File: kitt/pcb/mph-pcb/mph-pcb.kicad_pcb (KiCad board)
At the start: 4 copper layers, 280 x 125 mm, 10 parts

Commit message: changed pegboard holes to m5
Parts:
- PEG1, PEG2, PEG3, PEG4: value MountingHole_6.4mm_M6 -> MountingHole_5.3mm_M5; footprint MountingHole:MountingHole_6.4mm_M6 -> MountingHole:MountingHole_5.3mm_M5
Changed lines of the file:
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@@
     (uvia_drill 0.1)
   )
-  (module MountingHole:MountingHole_6.4mm_M6 (layer F.Cu)
+  (module MountingHole:MountingHole_5.3mm_M5 (layer F.Cu)
     (at 286.7 52.05)
-    (descr "Mounting Hole 6.4mm, no annular, M6")
-    (tags "mounting hole 6.4mm no annular m6")
+    (descr "Mounting Hole 5.3mm, no annular, M5")
+    (tags "mounting hole 5.3mm no annular m5")
     (attr virtual)
     (fp_text reference PEG2 (at 0 -7.4) (layer F.SilkS)
       (effects (font (size 1 1) (thickness 0.15)))
     )
-    (fp_text value MountingHole_6.4mm_M6 (at 0 7.4) (layer F.Fab)
+    (fp_text value MountingHole_5.3mm_M5 (at 0 7.4) (layer F.Fab)
       (effects (font (size 1 1) (thickness 0.15)))
     )
-    (fp_circle (center 0 0) (end 6.4 0) (layer Cmts.User) (width 0.15))
-    (fp_circle (center 0 0) (end 6.65 0) (layer F.CrtYd) (width 0.05))
     (fp_text user %R (at 0.3 0) (layer F.Fab)
       (effects (font (size 1 1) (thickness 0.15)))
     )
-    (pad 1 np_thru_hole circle (at 0 0) (size 6.4 6.4) (drill 6.4) (layers *.Cu *.Mask))
+    (fp_circle (center 0 0) (end 5.3 0) (layer Cmts.User) (width 0.15))
+    (fp_circle (center 0 0) (end 5.55 0) (layer F.CrtYd) (width 0.05))
+    (pad 1 np_thru_hole circle (at 0 0) (size 5.3 5.3) (drill 5.3) (layers *.Cu *.Mask))
   )
-  (module MountingHole:MountingHole_6.4mm_M6 (layer F.Cu)
+  (module MountingHole:MountingHole_5.3mm_M5 (layer F.Cu)
     (at 261.3 153.65)
-    (descr "Mounting Hole 6.4mm, no annular, M6")
-    (tags "mounting hole 6.4mm no annular m6")
+    (descr "Mounting Hole 5.3mm, no annular, M5")
+    (tags "mounting hole 5.3mm no annular m5")
     (attr virtual)
     (fp_text reference PEG4 (at 0 -7.4) (layer F.SilkS)
       (effects (font (size 1 1) (thickness 0.15)))
     )
-    (fp_text value MountingHole_6.4mm_M6 (at 0 7.4) (layer F.Fab)
+    (fp_text value MountingHole_5.3mm_M5 (at 0 7.4) (layer F.Fab)
       (effects (font (size 1 1) (thickness 0.15)))
     )
-    (fp_circle (center 0 0) (end 6.4 0) (layer Cmts.User) (width 0.15))
-    (fp_circle (center 0 0) (end 6.65 0) (layer F.CrtYd) (width 0.05))
     (fp_text user %R (at 0.3 0) (layer F.Fab)
       (effects (font (size 1 1) (thickness 0.15)))
     )
-    (pad 1 np_thru_hole circle (at 0 0) (size 6.4 6.4) (drill 6.4) (layers *.Cu *.Mask))
+    (fp_circle (center 0 0) (end 5.3 0) (layer Cmts.User) (width 0.15))
+    (fp_circle (center 0 0) (end 5.55 0) (layer F.CrtYd) (width 0.05))
+    (pad 1 np_thru_hole circle (at 0 0) (size 5.3 5.3) (drill 5.3) (layers *.Cu *.Mask))
   )
-  (module MountingHole:MountingHole_6.4mm_M6 (layer F.Cu)
+  (module MountingHole:MountingHole_5.3mm_M5 (layer F.Cu)
     (at 58.1 77.45)
-    (descr "Mounting Hole 6.4mm, no annular, M6")
-    (tags "mounting hole 6.4mm no annular m6")
+    (descr "Mounting Hole 5.3mm, no annular, M5")
+    (tags "mounting hole 5.3mm no annular m5")
     (attr virtual)
     (fp_text reference PEG1 (at 0 -7.4) (layer F.SilkS)
       (effects (font (size 1 1) (thickness 0.15)))
     )
-    (fp_text value MountingHole_6.4mm_M6 (at 0 7.4) (layer F.Fab)
+    (fp_text value MountingHole_5.3mm_M5 (at 0 7.4) (layer F.Fab)
       (effects (font (size 1 1) (thickness 0.15)))
     )
-    (fp_circle (center 0 0) (end 6.4 0) (layer Cmts.User) (width 0.15))
-    (fp_circle (center 0 0) (end 6.65 0) (layer F.CrtYd) (width 0.05))
     (fp_text user %R (at 0.3 0) (layer F.Fab)
       (effects (font (size 1 1) (thickness 0.15)))
     )
-    (pad 1 np_thru_hole circle (at 0 0) (size 6.4 6.4) (drill 6.4) (layers *.Cu *.Mask))
+    (fp_circle (center 0 0) (end 5.3 0) (layer Cmts.User) (width 0.15))
+    (fp_circle (center 0 0) (end 5.55 0) (layer F.CrtYd) (width 0.05))
+    (pad 1 np_thru_hole circle (at 0 0) (size 5.3 5.3) (drill 5.3) (layers *.Cu *.Mask))
   )
-  (module MountingHole:MountingHole_6.4mm_M6 (layer F.Cu)
+  (module MountingHole:MountingHole_5.3mm_M5 (layer F.Cu)
     (at 58.1 153.65)
-    (descr "Mounting Hole 6.4mm, no annular, M6")
-    (tags "mounting hole 6.4mm no annular m6")
+    (descr "Mounting Hole 5.3mm, no annular, M5")
+    (tags "mounting hole 5.3mm no annular m5")
     (attr virtual)
     (fp_text reference PEG3 (at 0 -7.4) (layer F.SilkS)
       (effects (font (size 1 1) (thickness 0.15)))
     )
-    (fp_text value MountingHole_6.4mm_M6 (at 0 7.4) (layer F.Fab)
+    (fp_text value MountingHole_5.3mm_M5 (at 0 7.4) (layer F.Fab)
       (effects (font (size 1 1) (thickness 0.15)))
     )
-    (fp_circle (center 0 0) (end 6.4 0) (layer Cmts.User) (width 0.15))
-    (fp_circle (center 0 0) (end 6.65 0) (layer F.CrtYd) (width 0.05))
     (fp_text user %R (at 0.3 0) (layer F.Fab)
       (effects (font (size 1 1) (thickness 0.15)))
     )
-    (pad 1 np_thru_hole circle (at 0 0) (size 6.4 6.4) (drill 6.4) (layers *.Cu *.Mask))
+    (fp_circle (center 0 0) (end 5.3 0) (layer Cmts.User) (width 0.15))
+    (fp_circle (center 0 0) (end 5.55 0) (layer F.CrtYd) (width 0.05))
+    (pad 1 np_thru_hole circle (at 0 0) (size 5.3 5.3) (drill 5.3) (layers *.Cu *.Mask))
   )
   (module MountingHole:MountingHole_3.2mm_M3 (layer F.Cu)
@@
       (effects (font (size 1 1) (thickness 0.15)))
     )
+    (fp_circle (center 0 0) (end 3.2 0) (layer Cmts.User) (width 0.15))
     (fp_circle (center 0 0) (end 3.45 0) (layer F.CrtYd) (width 0.05))
-    (fp_circle (center 0 0) (end 3.2 0) (layer Cmts.User) (width 0.15))
     (fp_text user %R (at 0.3 0) (layer F.Fab)
       (effects (font (size 1 1) (thickness 0.15)))
@@
       (effects (font (size 1 1) (thickness 0.15)))
     )
+    (fp_circle (center 0 0) (end 3.2 0) (layer Cmts.User) (width 0.15))
     (fp_circle (center 0 0) (end 3.45 0) (layer F.CrtYd) (width 0.05))
-    (fp_circle (center 0 0) (end 3.2 0) (layer Cmts.User) (width 0.15))
     (fp_text user %R (at 0.3 0) (layer F.Fab)
       (effects (font (size 1 1) (thickness 0.15)))
@@
       (effects (font (size 1 1) (thickness 0.15)))
     )
+    (fp_circle (center 0 0) (end 3.2 0) (layer Cmts.User) (width 0.15))
     (fp_circle (center 0 0) (end 3.45 0) (layer F.CrtYd) (width 0.05))
-    (fp_circle (center 0 0) (end 3.2 0) (layer Cmts.User) (width 0.15))
     (fp_text user %R (at 0.3 0) (layer F.Fab)
       (effects (font (size 1 1) (thickness 0.15)))
@@
       (effects (font (size 1 1) (thickness 0.15)))
     )
+    (fp_circle (center 0 0) (end 3.2 0) (layer Cmts.User) (width 0.15))
     (fp_circle (center 0 0) (end 3.45 0) (layer F.CrtYd) (width 0.05))
-    (fp_circle (center 0 0) (end 3.2 0) (layer Cmts.User) (width 0.15))
     (fp_text user %R (at 0.3 0) (layer F.Fab)
       (effects (font (size 1 1) (thickness 0.15)))
@@
       (effects (font (size 1 1) (thickness 0.15)))
     )
+    (fp_circle (center 0 0) (end 3.2 0) (layer Cmts.User) (width 0.15))
     (fp_circle (center 0 0) (end 3.45 0) (layer F.CrtYd) (width 0.05))
-    (fp_circle (center 0 0) (end 3.2 0) (layer Cmts.User) (width 0.15))
     (fp_text user %R (at 0.3 0) (layer F.Fab)
       (effects (font (size 1 1) (thickness 0.15)))
@@
       (effects (font (size 1 1) (thickness 0.15)))
     )
+    (fp_circle (center 0 0) (end 3.2 0) (layer Cmts.User) (width 0.15))
     (fp_circle (center 0 0) (end 3.45 0) (layer F.CrtYd) (width 0.05))
-    (fp_circle (center 0 0) (end 3.2 0) (layer Cmts.User) (width 0.15))
     (fp_text user %R (at 0.3 0) (layer F.Fab)
       (effects (font (size 1 1) (thickness 0.15)))

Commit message: initial placement
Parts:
- added C1: 100nF, Capacitor_THT:C_Rect_L7.0mm_W3.5mm_P5.00mm, F.Cu at (176.0, -43.4)
- added C2: 1uF, Capacitor_THT:C_Rect_L7.0mm_W3.5mm_P5.00mm, F.Cu at (204.5, 24.1)
- added C3: 100nF, Capacitor_THT:C_Rect_L7.0mm_W3.5mm_P5.00mm, F.Cu at (271.7, -41.7)
- added C4: 100nF, Capacitor_THT:C_Rect_L7.0mm_W3.5mm_P5.00mm, F.Cu at (284.5, -53.9)
- added C5: 100nF, Capacitor_THT:C_Rect_L7.0mm_W3.5mm_P5.00mm, F.Cu at (176.0, -38.3)
- added C6: 100nF, Capacitor_THT:C_Rect_L7.0mm_W3.5mm_P5.00mm, F.Cu at (255.7, -16.0)
- added C7: 100nF, Capacitor_THT:C_Rect_L7.0mm_W3.5mm_P5.00mm, F.Cu at (293.0, -53.9)
- added C8: 100nF, Capacitor_THT:C_Rect_L7.0mm_W3.5mm_P5.00mm, F.Cu at (284.5, -48.8)
- added C9: 100nF, Capacitor_THT:C_Rect_L7.0mm_W3.5mm_P5.00mm, F.Cu at (280.2, -41.7)
- added D25: LED, KITT-Footpads:Flangeless_LED, F.Cu at (275.6, -30.0)
- added D26: LED, KITT-Footpads:Flangeless_LED, F.Cu at (283.9, -36.2)
- added D27: LED, KITT-Footpads:Flangeless_LED, F.Cu at (292.7, 6.62)
- added GUID1: DF3GD, KITT-Footpads:DF3GD_Light_Bar, F.Cu at (103.4, 80.3)
- added GUID2: DF3GD, KITT-Footpads:DF3GD_Light_Bar, F.Cu at (123.8, 80.3)
- added HT1: LED, KITT-Footpads:Flangeless_LED, F.Cu at (293.0, -48.3)
- added HT10: LED, KITT-Footpads:Flangeless_LED, F.Cu at (287.8, -23.8)
- added HT11: LED, KITT-Footpads:Flangeless_LED, F.Cu at (277.8, -36.2)
- added HT12: LED, KITT-Footpads:Flangeless_LED, F.Cu at (245.8, -4.34)
- added HT13: LED, KITT-Footpads:Flangeless_LED, F.Cu at (240.7, 3.35)
- added HT14: LED, KITT-Footpads:Flangeless_LED, F.Cu at (228.8, 13.0)
- added HT15: LED, KITT-Footpads:Flangeless_LED, F.Cu at (223.9, 19.1)
- added HT16: LED, KITT-Footpads:Flangeless_LED, F.Cu at (251.9, -10.4)
- added HT2: LED, KITT-Footpads:Flangeless_LED, F.Cu at (230.0, 19.1)
- added HT3: LED, KITT-Footpads:Flangeless_LED, F.Cu at (301.6, -58.5)
- added HT4: LED, KITT-Footpads:Flangeless_LED, F.Cu at (251.9, -4.27)
- added HT5: LED, KITT-Footpads:Flangeless_LED, F.Cu at (258.0, -10.4)
- added HT6: LED, KITT-Footpads:Flangeless_LED, F.Cu at (271.7, -36.2)
- added HT7: LED, KITT-Footpads:Flangeless_LED, F.Cu at (245.8, -10.5)
- added HT8: LED, KITT-Footpads:Flangeless_LED, F.Cu at (234.6, 3.35)
- added HT9: LED, KITT-Footpads:Flangeless_LED, F.Cu at (234.9, 9.47)
- added HY1: LED, KITT-Footpads:Flangeless_LED, F.Cu at (217.8, 20.5)
- added HY2: LED, KITT-Footpads:Flangeless_LED, F.Cu at (222.7, 13.0)
- added HY3: LED, KITT-Footpads:Flangeless_LED, F.Cu at (269.4, -28.5)
- added J1: Screw_Terminal_01x02, KITT-Footpads:5mm_Screw_Terminal_01x02, F.Cu at (151.7, 148.9)
- added J2: Screw_Terminal_01x03, KITT-Footpads:5mm_Screw_Terminal_01x03, F.Cu at (253.3, 142.5)
- added LVL1: LVL_5V_3V3, KITT-Footpads:LVL_5V_3V3, F.Cu at (238.1, 141.2)
- added MASH_DISP1: LDS-A816RI, KITT-Footpads:LDS-A816RI, F.Cu at (51.4, 117.1)
- added MASH_DISP2: LDS-A816RI, KITT-Footpads:LDS-A816RI, F.Cu at (71.7, 117.1)
- added MASH_DISP3: LDS-A816RI, KITT-Footpads:LDS-A816RI, F.Cu at (92.0, 117.1)
- added MASH_DISP4: LDS-A816RI, KITT-Footpads:LDS-A816RI, F.Cu at (112.3, 117.1)
- added MPH1: KB2855SGD, KITT-Footpads:KB2855SGD_Light_Square, F.Cu at (224.1, 84.1)
- added MPH2: KB2855SGD, KITT-Footpads:KB2855SGD_Light_Square, F.Cu at (234.2, 84.1)
- added MPH3: KB2855SGD, KITT-Footpads:KB2855SGD_Light_Square, F.Cu at (244.4, 84.1)
- added MY1: LED, KITT-Footpads:Flangeless_LED, F.Cu at (301.6, -52.4)
- added MY2: LED, KITT-Footpads:Flangeless_LED, F.Cu at (253.3, 7.97)
- added MY3: LED, KITT-Footpads:Flangeless_LED, F.Cu at (293.9, -29.9)
- added PWR1: OKI-78SR-5_1.5-W36H-C, Converter_DCDC:Converter_DCDC_muRata_OKI-78SR_Horizontal, F.Cu at (163.1, 148.9)
- added R1: 2.2K, Resistor_THT:R_Axial_DIN0207_L6.3mm_D2.5mm_P10.16mm_Horizontal, F.Cu at (284.3, -66.5)
- added R10: 120R, Resistor_THT:R_Axial_DIN0207_L6.3mm_D2.5mm_P10.16mm_Horizontal, F.Cu at (209.2, 15.4)
- added R11: 120R, Resistor_THT:R_Axial_DIN0207_L6.3mm_D2.5mm_P10.16mm_Horizontal, F.Cu at (258.2, -33.6)
- added R12: 120R, Resistor_THT:R_Axial_DIN0207_L6.3mm_D2.5mm_P10.16mm_Horizontal, F.Cu at (271.0, -46.3)
- added R13: 120R, Resistor_THT:R_Axial_DIN0207_L6.3mm_D2.5mm_P10.16mm_Horizontal, F.Cu at (284.3, -58.4)
- added R14: 120R, Resistor_THT:R_Axial_DIN0207_L6.3mm_D2.5mm_P10.16mm_Horizontal, F.Cu at (132.4, 22.2)
- added R15: 120R, Resistor_THT:R_Axial_DIN0207_L6.3mm_D2.5mm_P10.16mm_Horizontal, F.Cu at (191.0, 23.6)
- added R16: 120R, Resistor_THT:R_Axial_DIN0207_L6.3mm_D2.5mm_P10.16mm_Horizontal, F.Cu at (191.0, 19.6)
- added R17: 120R, Resistor_THT:R_Axial_DIN0207_L6.3mm_D2.5mm_P10.16mm_Horizontal, F.Cu at (271.0, -66.5)
- added R18: 120R, Resistor_THT:R_Axial_DIN0207_L6.3mm_D2.5mm_P10.16mm_Horizontal, F.Cu at (209.2, 7.28)
- added R19: 120R, Resistor_THT:R_Axial_DIN0207_L6.3mm_D2.5mm_P10.16mm_Horizontal, F.Cu at (271.0, -54.4)
- added R2: 2.2K, Resistor_THT:R_Axial_DIN0207_L6.3mm_D2.5mm_P10.16mm_Horizontal, F.Cu at (221.0, -0.82)
- added R20: 120R, Resistor_THT:R_Axial_DIN0207_L6.3mm_D2.5mm_P10.16mm_Horizontal, F.Cu at (242.4, -24.6)
- added R21: 120R, Resistor_THT:R_Axial_DIN0207_L6.3mm_D2.5mm_P10.16mm_Horizontal, F.Cu at (258.2, -41.7)
- added R22: 120R, Resistor_THT:R_Axial_DIN0207_L6.3mm_D2.5mm_P10.16mm_Horizontal, F.Cu at (221.2, -4.87)
- added R23: 120R, Resistor_THT:R_Axial_DIN0207_L6.3mm_D2.5mm_P10.16mm_Horizontal, F.Cu at (229.1, -19.6)
- added R24: 120R, Resistor_THT:R_Axial_DIN0207_L6.3mm_D2.5mm_P10.16mm_Horizontal, F.Cu at (195.9, 15.5)
- added R25: 120R, Resistor_THT:R_Axial_DIN0207_L6.3mm_D2.5mm_P10.16mm_Horizontal, F.Cu at (271.0, -58.4)
- added R26: 120R, Resistor_THT:R_Axial_DIN0207_L6.3mm_D2.5mm_P10.16mm_Horizontal, F.Cu at (145.8, 22.2)
- added R27: 120R, Resistor_THT:R_Axial_DIN0207_L6.3mm_D2.5mm_P10.16mm_Horizontal, F.Cu at (209.2, 3.23)
- added R28: 120R, Resistor_THT:R_Axial_DIN0207_L6.3mm_D2.5mm_P10.16mm_Horizontal, F.Cu at (271.0, -62.5)
- added R29: 120R, Resistor_THT:R_Axial_DIN0207_L6.3mm_D2.5mm_P10.16mm_Horizontal, F.Cu at (195.9, 11.5)
- added R3: 2.2K, Resistor_THT:R_Axial_DIN0207_L6.3mm_D2.5mm_P10.16mm_Horizontal, F.Cu at (242.2, -15.5)
- added R30: 120R, Resistor_THT:R_Axial_DIN0207_L6.3mm_D2.5mm_P10.16mm_Horizontal, F.Cu at (284.3, -70.6)
- added R31: 120R, Resistor_THT:R_Axial_DIN0207_L6.3mm_D2.5mm_P10.16mm_Horizontal, F.Cu at (228.9, -12.8)
- added R32: 10K, Resistor_THT:R_Axial_DIN0207_L6.3mm_D2.5mm_P10.16mm_Horizontal, F.Cu at (271.0, -70.6)
- added R33: 10K, Resistor_THT:R_Axial_DIN0207_L6.3mm_D2.5mm_P10.16mm_Horizontal, F.Cu at (195.9, 7.43)
- added R34: 10K, Resistor_THT:R_Axial_DIN0207_L6.3mm_D2.5mm_P10.16mm_Horizontal, F.Cu at (207.7, -0.82)
- added R35: 10K, Resistor_THT:R_Axial_DIN0207_L6.3mm_D2.5mm_P10.16mm_Horizontal, F.Cu at (195.9, 3.38)
- added R36: 10K, Resistor_THT:R_Axial_DIN0207_L6.3mm_D2.5mm_P10.16mm_Horizontal, F.Cu at (207.9, -4.87)
- added R37: 10K, Resistor_THT:R_Axial_DIN0207_L6.3mm_D2.5mm_P10.16mm_Horizontal, F.Cu at (229.1, -23.6)
- added R38: 10K, Resistor_THT:R_Axial_DIN0207_L6.3mm_D2.5mm_P10.16mm_Horizontal, F.Cu at (159.1, 22.2)
- added R4: 2.2K, Resistor_THT:R_Axial_DIN0207_L6.3mm_D2.5mm_P10.16mm_Horizontal, F.Cu at (284.3, -62.5)
- added R5: 2.2K, Resistor_THT:R_Axial_DIN0207_L6.3mm_D2.5mm_P10.16mm_Horizontal, F.Cu at (271.0, -50.3)
- added R6: 2.2K, Resistor_THT:R_Axial_DIN0207_L6.3mm_D2.5mm_P10.16mm_Horizontal, F.Cu at (242.4, -20.5)
- added R7: 2.2K, Resistor_THT:R_Axial_DIN0207_L6.3mm_D2.5mm_P10.16mm_Horizontal, F.Cu at (258.2, -37.6)
- added R8: 120R, Resistor_THT:R_Axial_DIN0207_L6.3mm_D2.5mm_P10.16mm_Horizontal, F.Cu at (209.2, 11.3)
- added R9: 120R, Resistor_THT:R_Axial_DIN0207_L6.3mm_D2.5mm_P10.16mm_Horizontal, F.Cu at (204.3, 19.6)
- added SYST1: DF3GD, KITT-Footpads:DF3GD_Light_Bar, F.Cu at (90.7, 91.7)
- added SYST2: DF3GD, KITT-Footpads:DF3GD_Light_Bar, F.Cu at (111.0, 91.7)
- added THRU1: MountingHole_6.4mm_M6, MountingHole:MountingHole_6.4mm_M6, F.Cu at (119.9, 152.7)
- added THRU2: MountingHole_6.4mm_M6, MountingHole:MountingHole_6.4mm_M6, F.Cu at (282.5, 118.4)
- added TTGO1: TTGO_ESP32_TDISPLAY_V1.1, KITT-Footpads:TTGO_ESP32_TDisplay_v1.1, F.Cu at (293.9, 96.8)
- added U1: TLC5940NT, Package_DIP:DIP-28_W7.62mm, F.Cu at (196.6, -70.5)
- added U2: TLC5940NT, Package_DIP:DIP-28_W7.62mm, F.Cu at (175.9, -33.4)
- added U3: TLC5940NT, Package_DIP:DIP-28_W7.62mm, F.Cu at (165.0, -43.8)
- added U4: TLC5940NT, Package_DIP:DIP-28_W7.62mm, F.Cu at (154.2, -43.8)
- added U5: TLC5940NT, Package_DIP:DIP-28_W7.62mm, F.Cu at (143.3, -43.8)
- added U6: TLC5940NT, Package_DIP:DIP-28_W7.62mm, F.Cu at (185.7, -70.5)
- added U7: TLC5940NT, Package_DIP:DIP-28_W7.62mm, F.Cu at (132.5, -43.8)
- added UG1: LED, KITT-Footpads:Flangeless_LED, F.Cu at (246.8, 1.85)
- added UG10: LED, KITT-Footpads:Flangeless_LED, F.Cu at (290.1, -36.1)
- added UG11: LED, KITT-Footpads:Flangeless_LED, F.Cu at (252.9, 1.85)
- added UG12: LED, KITT-Footpads:Flangeless_LED, F.Cu at (236.2, 15.6)
- added UG13: LED, KITT-Footpads:Flangeless_LED, F.Cu at (247.2, 7.97)
- added UG14: LED, KITT-Footpads:Flangeless_LED, F.Cu at (264.2, -5.21)
- added UG15: LED, KITT-Footpads:Flangeless_LED, F.Cu at (242.3, 15.6)
- added UG16: LED, KITT-Footpads:Flangeless_LED, F.Cu at (236.2, 21.7)
- added UG17: LED, KITT-Footpads:Flangeless_LED, F.Cu at (276.5, -17.8)
- added UG18: LED, KITT-Footpads:Flangeless_LED, F.Cu at (270.4, -11.7)
- added UG19: LED, KITT-Footpads:Flangeless_LED, F.Cu at (281.7, -23.9)
- added UG2: LED, KITT-Footpads:Flangeless_LED, F.Cu at (290.1, -42.2)
- added UG20: LED, KITT-Footpads:Flangeless_LED, F.Cu at (296.2, -36.1)
- added UG3: LED, KITT-Footpads:Flangeless_LED, F.Cu at (241.1, 9.47)
- added UG4: LED, KITT-Footpads:Flangeless_LED, F.Cu at (264.3, -11.3)
- added UG5: LED, KITT-Footpads:Flangeless_LED, F.Cu at (281.7, -30.0)
- added UG6: LED, KITT-Footpads:Flangeless_LED, F.Cu at (275.6, -23.9)
- added UG7: LED, KITT-Footpads:Flangeless_LED, F.Cu at (270.4, -17.8)
- added UG8: LED, KITT-Footpads:Flangeless_LED, F.Cu at (258.0, -4.27)
- added UG9: LED, KITT-Footpads:Flangeless_LED, F.Cu at (296.2, -42.2)
- added UGY1: LED, KITT-Footpads:Flangeless_LED, F.Cu at (302.3, -46.3)
- added UGY2: LED, KITT-Footpads:Flangeless_LED, F.Cu at (287.8, -29.9)
- added UGY3: LED, KITT-Footpads:Flangeless_LED, F.Cu at (259.0, 1.85)
- added UT_DISP1: LDS-A816RI, KITT-Footpads:LDS-A816RI, F.Cu at (155.5, 70.1)
- added UT_DISP2: LDS-A816RI, KITT-Footpads:LDS-A816RI, F.Cu at (175.8, 70.1)
- added UT_DISP3: LDS-A816RI, KITT-Footpads:LDS-A816RI, F.Cu at (196.1, 70.1)
- moved PEG2 29.6 mm to (257.1, 52.0)
- moved PEG4 25.9 mm to (282.5, 138.7)

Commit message: finished placing leds
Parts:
- moved MY1 294.8 mm to (48.8, 99.3)
- moved HT3 291.6 mm to (61.5, 107.0)
- moved HT1 287.3 mm to (51.4, 107.0)
- moved MY3 268.2 mm to (59.0, 99.3)
- moved HT6 241.8 mm to (76.8, 107.0)
- moved HT10 231.3 mm to (97.1, 107.0)
- moved HT11 226.6 mm to (102.2, 107.0)
- moved HT5 220.2 mm to (71.7, 107.0)
- moved MY2 219.3 mm to (53.9, 99.3)
- moved HT4 216.1 mm to (66.6, 107.0)
- moved HT7 201.7 mm to (81.8, 107.0)
- moved HT2 194.6 mm to (56.4, 107.0)
- moved MSGY2 183.2 mm to (160.6, 99.3)
- moved HT8 180.4 mm to (86.9, 107.0)
- moved HT12 177.7 mm to (107.2, 107.0)
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- renumbered D25 to MSGY1, D26 to MSGY2, D27 to MSGY3

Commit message: place chips and resistors
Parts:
- moved R32 331.4 mm to (31.5, 158.5)
- moved R1 306.7 mm to (24.7, 96.8), turned to 270 degrees
- moved C3 302.2 mm to (24.7, 132.3), turned to 90 degrees
- moved U1 272.1 mm to (37.4, 150.1), turned to 180 degrees
- moved R17 218.8 mm to (95.2, 63.8), turned to 270 degrees
- moved R13 217.2 mm to (104.7, 63.8), turned to 270 degrees
- moved R19 206.6 mm to (101.5, 63.8), turned to 270 degrees
- moved R12 196.8 mm to (107.9, 63.8), turned to 270 degrees
- moved U3 190.6 mm to (32.3, 93.0), turned to 90 degrees
- moved U7 186.5 mm to (252.0, 99.3), turned to 270 degrees
- moved U6 177.8 mm to (174.6, 107.0), turned to 90 degrees
- moved R11 176.4 mm to (111.0, 63.8), turned to 270 degrees
- moved U2 158.7 mm to (139.0, 120.9)
- moved R10 141.6 mm to (76.1, 63.8), turned to 270 degrees
- moved R30 141.1 mm to (250.1, 66.3), turned to 270 degrees
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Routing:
- added copper zone on In1.Cu, net +5V

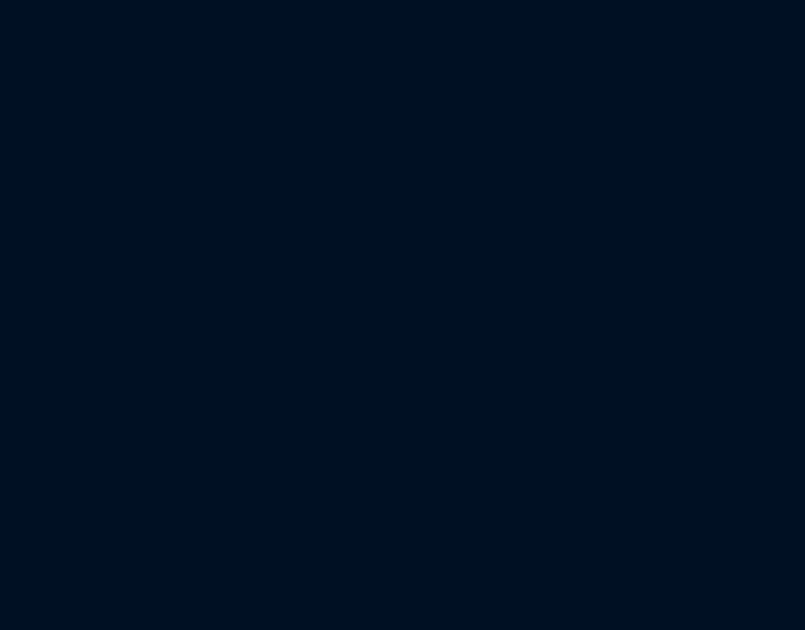
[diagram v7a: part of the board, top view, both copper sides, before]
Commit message: add net ties for coupling caps
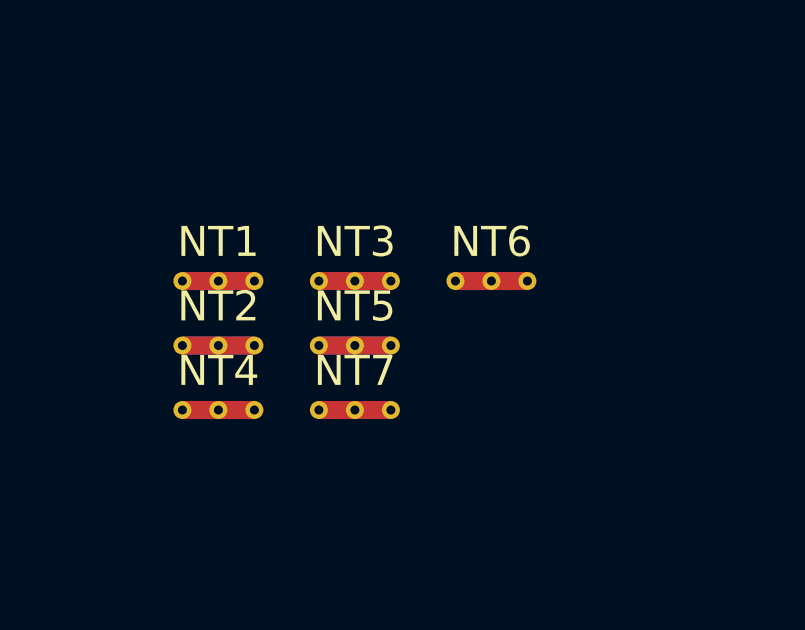
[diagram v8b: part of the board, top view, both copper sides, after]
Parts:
- added NT1: Net-Tie_3_Tee, NetTie:NetTie-3_THT_Pad0.3mm, F.Cu at (24.1, 36.5)
- added NT2: Net-Tie_3_Tee, NetTie:NetTie-3_THT_Pad0.3mm, F.Cu at (24.1, 38.6)
- added NT3: Net-Tie_3_Tee, NetTie:NetTie-3_THT_Pad0.3mm, F.Cu at (28.6, 36.5)
- added NT4: Net-Tie_3_Tee, NetTie:NetTie-3_THT_Pad0.3mm, F.Cu at (24.1, 40.8)
- added NT5: Net-Tie_3_Tee, NetTie:NetTie-3_THT_Pad0.3mm, F.Cu at (28.6, 38.6)
- added NT6: Net-Tie_3_Tee, NetTie:NetTie-3_THT_Pad0.3mm, F.Cu at (33.2, 36.5)
- added NT7: Net-Tie_3_Tee, NetTie:NetTie-3_THT_Pad0.3mm, F.Cu at (28.6, 40.8)
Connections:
- C3 pad 1: +5V -> Net-(C3-Pad1)
- C4 pad 1: +5V -> Net-(C4-Pad1)
- C5 pad 1: +5V -> Net-(C5-Pad1)
- C6 pad 1: +5V -> Net-(C6-Pad1)
- C7 pad 1: +5V -> Net-(C7-Pad1)
- C8 pad 1: +5V -> Net-(C8-Pad1)
- C9 pad 1: +5V -> Net-(C9-Pad1)
- U1 pad 21: +5V -> Net-(NT1-Pad2)
- U2 pad 21: +5V -> Net-(NT2-Pad2)
- U3 pad 21: +5V -> Net-(NT3-Pad2)
- U4 pad 21: +5V -> Net-(NT4-Pad2)
- U5 pad 21: +5V -> Net-(NT5-Pad2)
- U6 pad 21: +5V -> Net-(NT6-Pad2)
- U7 pad 21: +5V -> Net-(NT7-Pad2)
